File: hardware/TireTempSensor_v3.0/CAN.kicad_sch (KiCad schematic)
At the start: 14 parts, among them U7 ADM3057ExRW

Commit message: Poprawki, kontynuacja layoutu
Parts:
- C32, C38: value 100n -> 47u
- C35: value 220n -> 47u
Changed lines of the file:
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@@
 	(polyline
 		(pts
-			(xy 108.585 17.145) (xy 107.95 193.04)
+			(xy 108.585 45.085) (xy 108.585 104.14)
 		)
 		(stroke
@@
 			)
 		)
-		(property "Value" "100n"
+		(property "Value" "47u"
 			(at 150.5013 22.225 90)
 			(effects
@@
 			)
 		)
-		(property "Value" "220n"
+		(property "Value" "47u"
 			(at 85.725 79.3685 0)
 			(effects
@@
 			)
 		)
-		(property "Value" "100n"
+		(property "Value" "47u"
 			(at 118.7513 22.225 90)
 			(effects

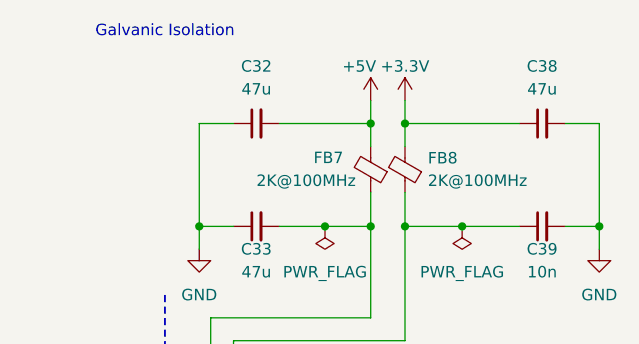
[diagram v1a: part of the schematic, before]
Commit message: Nowy layout, nowe tvsy
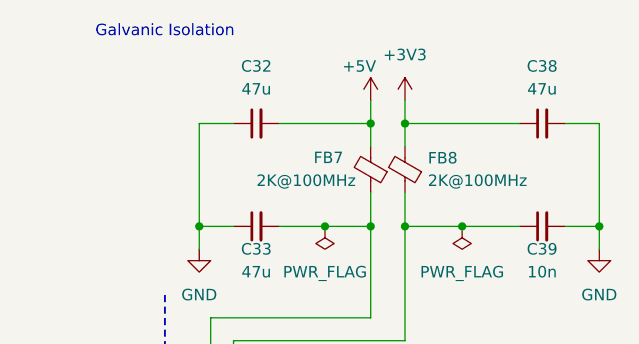
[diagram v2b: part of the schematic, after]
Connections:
- net +3.3V renamed +3V3
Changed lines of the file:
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@@
+	)
+	(symbol
+		(lib_id "power:+3V3")
+		(at 135.255 23.495 0)
+		(unit 1)
+		(exclude_from_sim no)
+		(in_bom yes)
+		(on_board yes)
+		(dnp no)
+		(fields_autoplaced yes)
+		(property "Reference" "#PWR0119"
+			(at 135.255 27.305 0)
+			(effects
+				(font
+					(size 1.27 1.27)
+				)
+				(hide yes)
+			)
+		)
+		(property "Value" "+3V3"
+			(at 135.255 18.415 0)
+			(effects
+				(font
+					(size 1.27 1.27)
+				)
+			)
+		)
+		(property "Footprint" ""
+			(at 135.255 23.495 0)
+			(effects
+				(font
+					(size 1.27 1.27)
+				)
+				(hide yes)
+			)
+		)
+		(property "Datasheet" ""
+			(at 135.255 23.495 0)
+			(effects
+				(font
+					(size 1.27 1.27)
+				)
+				(hide yes)
+			)
+		)
+		(property "Description" ""
+			(at 135.255 23.495 0)
+			(effects
+				(font
+					(size 1.27 1.27)
+				)
+			)
+		)
+		(pin "1"
+		)
+		(instances
+			(project "TireTempSensor_v2.0"
+				(path "/6e95e1be-fdd6-40ae-a4f8-5c53e6058d6c/4ba3e466-bd12-480c-9adb-36d880e66258"
+					(reference "#PWR0119")
+					(unit 1)
+				)
+			)
+		)
 	)
 	(symbol
@@
 					(unit 1)
 				)
-			)
-		)
-	)
-	(symbol
-		(lib_id "power:+3.3V")
-		(at 135.255 23.495 0)
-		(unit 1)
-		(exclude_from_sim no)
-		(in_bom yes)
-		(on_board yes)
-		(dnp no)
-		(fields_autoplaced yes)
-		(property "Reference" "#PWR062"
-			(at 135.255 27.305 0)
-			(effects
-				(font
-					(size 1.27 1.27)
-				)
-				(hide yes)
-			)
-		)
-		(property "Value" "+3.3V"
-			(at 135.255 19.685 0)
-			(effects
-				(font
-					(size 1.27 1.27)
-				)
-			)
-		)
-		(property "Footprint" ""
-			(at 135.255 23.495 0)
-			(effects
-				(font
-					(size 1.27 1.27)
-				)
-				(hide yes)
-			)
-		)
-		(property "Datasheet" ""
-			(at 135.255 23.495 0)
-			(effects
-				(font
-					(size 1.27 1.27)
-				)
-				(hide yes)
-			)
-		)
-		(property "Description" ""
-			(at 135.255 23.495 0)
-			(effects
-				(font
-					(size 1.27 1.27)
-				)
-				(hide yes)
-			)
-		)
-		(pin "1"
-		)
-		(instances
-			(project "TireTempSensor_v2.0"
-				(path "/6e95e1be-fdd6-40ae-a4f8-5c53e6058d6c/4ba3e466-bd12-480c-9adb-36d880e66258"
-					(reference "#PWR062")
-					(unit 1)
-				)

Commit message: Poprawione :3
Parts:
- C32, C33, C34, C38: footprint Capacitor_SMD:C_0603_1608Metric_Pad1.08x0.95mm_HandSolder -> Capacitor_SMD:C_0805_2012Metric_Pad1.18x1.45mm_HandSolder
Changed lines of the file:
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@@
 			)
 		)
-		(property "Footprint" "Capacitor_SMD:C_0603_1608Metric_Pad1.08x0.95mm_HandSolder"
+		(property "Footprint" "Capacitor_SMD:C_0805_2012Metric_Pad1.18x1.45mm_HandSolder"
 			(at 118.745 37.465 0)
 			(effects
@@
 			)
 		)
-		(property "Footprint" "Capacitor_SMD:C_0603_1608Metric_Pad1.08x0.95mm_HandSolder"
+		(property "Footprint" "Capacitor_SMD:C_0805_2012Metric_Pad1.18x1.45mm_HandSolder"
 			(at 150.495 26.035 0)
 			(effects
@@
 			)
 		)
-		(property "Footprint" "Capacitor_SMD:C_0603_1608Metric_Pad1.08x0.95mm_HandSolder"
+		(property "Footprint" "Capacitor_SMD:C_0805_2012Metric_Pad1.18x1.45mm_HandSolder"
 			(at 65.405 78.105 0)
 			(effects
@@
 			)
 		)
-		(property "Footprint" "Capacitor_SMD:C_0603_1608Metric_Pad1.08x0.95mm_HandSolder"
+		(property "Footprint" "Capacitor_SMD:C_0805_2012Metric_Pad1.18x1.45mm_HandSolder"
 			(at 118.745 26.035 0)
 			(effects

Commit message: Piotrkowe poprawy
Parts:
- FB5, FB6, FB7, FB8: footprint Inductor_SMD:L_0603_1608Metric_Pad1.05x0.95mm_HandSolder -> Inductor_SMD:L_0805_2012Metric_Pad1.05x1.20mm_HandSolder
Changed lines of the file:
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@@
 			)
 		)
-		(property "Footprint" "Inductor_SMD:L_0603_1608Metric_Pad1.05x0.95mm_HandSolder"
+		(property "Footprint" "Inductor_SMD:L_0805_2012Metric_Pad1.05x1.20mm_HandSolder"
 			(at 137.033 31.115 90)
 			(effects
@@
 			)
 		)
-		(property "Datasheet" "https://www.mouser.pl/ProductDetail/Eaton-Electronics/MFBW1V1608-202-R?qs=W%2FMpXkg%252BdQ4ShGRk3jgFwA%3D%3D"
+		(property "Datasheet" "https://www.mouser.pl/ProductDetail/Fair-Rite/2508052027Y1?qs=paL1wOLBYNcCgyNDp2sTMQ%3D%3D"
 			(at 135.255 31.115 0)
 			(effects
@@
 			)
 		)
-		(property "Footprint" "Inductor_SMD:L_0603_1608Metric_Pad1.05x0.95mm_HandSolder"
+		(property "Footprint" "Inductor_SMD:L_0805_2012Metric_Pad1.05x1.20mm_HandSolder"
 			(at 133.223 31.115 90)
 			(effects
@@
 			)
 		)
-		(property "Datasheet" "https://www.mouser.pl/ProductDetail/Eaton-Electronics/MFBW1V1608-202-R?qs=W%2FMpXkg%252BdQ4ShGRk3jgFwA%3D%3D"
+		(property "Datasheet" "https://www.mouser.pl/ProductDetail/Fair-Rite/2508052027Y1?qs=paL1wOLBYNcCgyNDp2sTMQ%3D%3D"
 			(at 131.445 31.115 0)
 			(effects
@@
 					(size 1.27 1.27)
 				)
-			)
-		)
-		(property "Footprint" "Inductor_SMD:L_0603_1608Metric_Pad1.05x0.95mm_HandSolder"
+				(justify right)
+			)
+		)
+		(property "Footprint" "Inductor_SMD:L_0805_2012Metric_Pad1.05x1.20mm_HandSolder"
 			(at 74.295 77.343 90)
 			(effects
@@
 			)
 		)
-		(property "Datasheet" "https://www.mouser.pl/ProductDetail/Eaton-Electronics/MFBW1V1608-202-R?qs=W%2FMpXkg%252BdQ4ShGRk3jgFwA%3D%3D"
+		(property "Datasheet" "https://www.mouser.pl/ProductDetail/Fair-Rite/2508052027Y1?qs=paL1wOLBYNcCgyNDp2sTMQ%3D%3D"
 			(at 74.295 75.565 0)
 			(effects
@@
 		)
 		(property "Value" "2K@100MHz"
-			(at 73.025 84.455 90)
-			(effects
-				(font
-					(size 1.27 1.27)
-				)
-			)
-		)
-		(property "Footprint" "Inductor_SMD:L_0603_1608Metric_Pad1.05x0.95mm_HandSolder"
+			(at 67.945 84.455 90)
+			(effects
+				(font
+					(size 1.27 1.27)
+				)
+				(justify right)
+			)
+		)
+		(property "Footprint" "Inductor_SMD:L_0805_2012Metric_Pad1.05x1.20mm_HandSolder"
 			(at 74.295 82.423 90)
 			(effects
@@
 			)
 		)
-		(property "Datasheet" "https://www.mouser.pl/ProductDetail/Eaton-Electronics/MFBW1V1608-202-R?qs=W%2FMpXkg%252BdQ4ShGRk3jgFwA%3D%3D"
+		(property "Datasheet" "https://www.mouser.pl/ProductDetail/Fair-Rite/2508052027Y1?qs=paL1wOLBYNcCgyNDp2sTMQ%3D%3D"
 			(at 74.295 80.645 0)
 			(effects

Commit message: Z wielkim bólem przesunięte złącze aby poprawić routing cana
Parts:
- C35: footprint Capacitor_SMD:C_0603_1608Metric_Pad1.08x0.95mm_HandSolder -> Capacitor_SMD:C_0805_2012Metric_Pad1.18x1.45mm_HandSolder
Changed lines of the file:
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@@
 			)
 		)
-		(property "Footprint" "Capacitor_SMD:C_0603_1608Metric_Pad1.08x0.95mm_HandSolder"
+		(property "Footprint" "Capacitor_SMD:C_0805_2012Metric_Pad1.18x1.45mm_HandSolder"
 			(at 83.185 78.105 0)
 			(effects

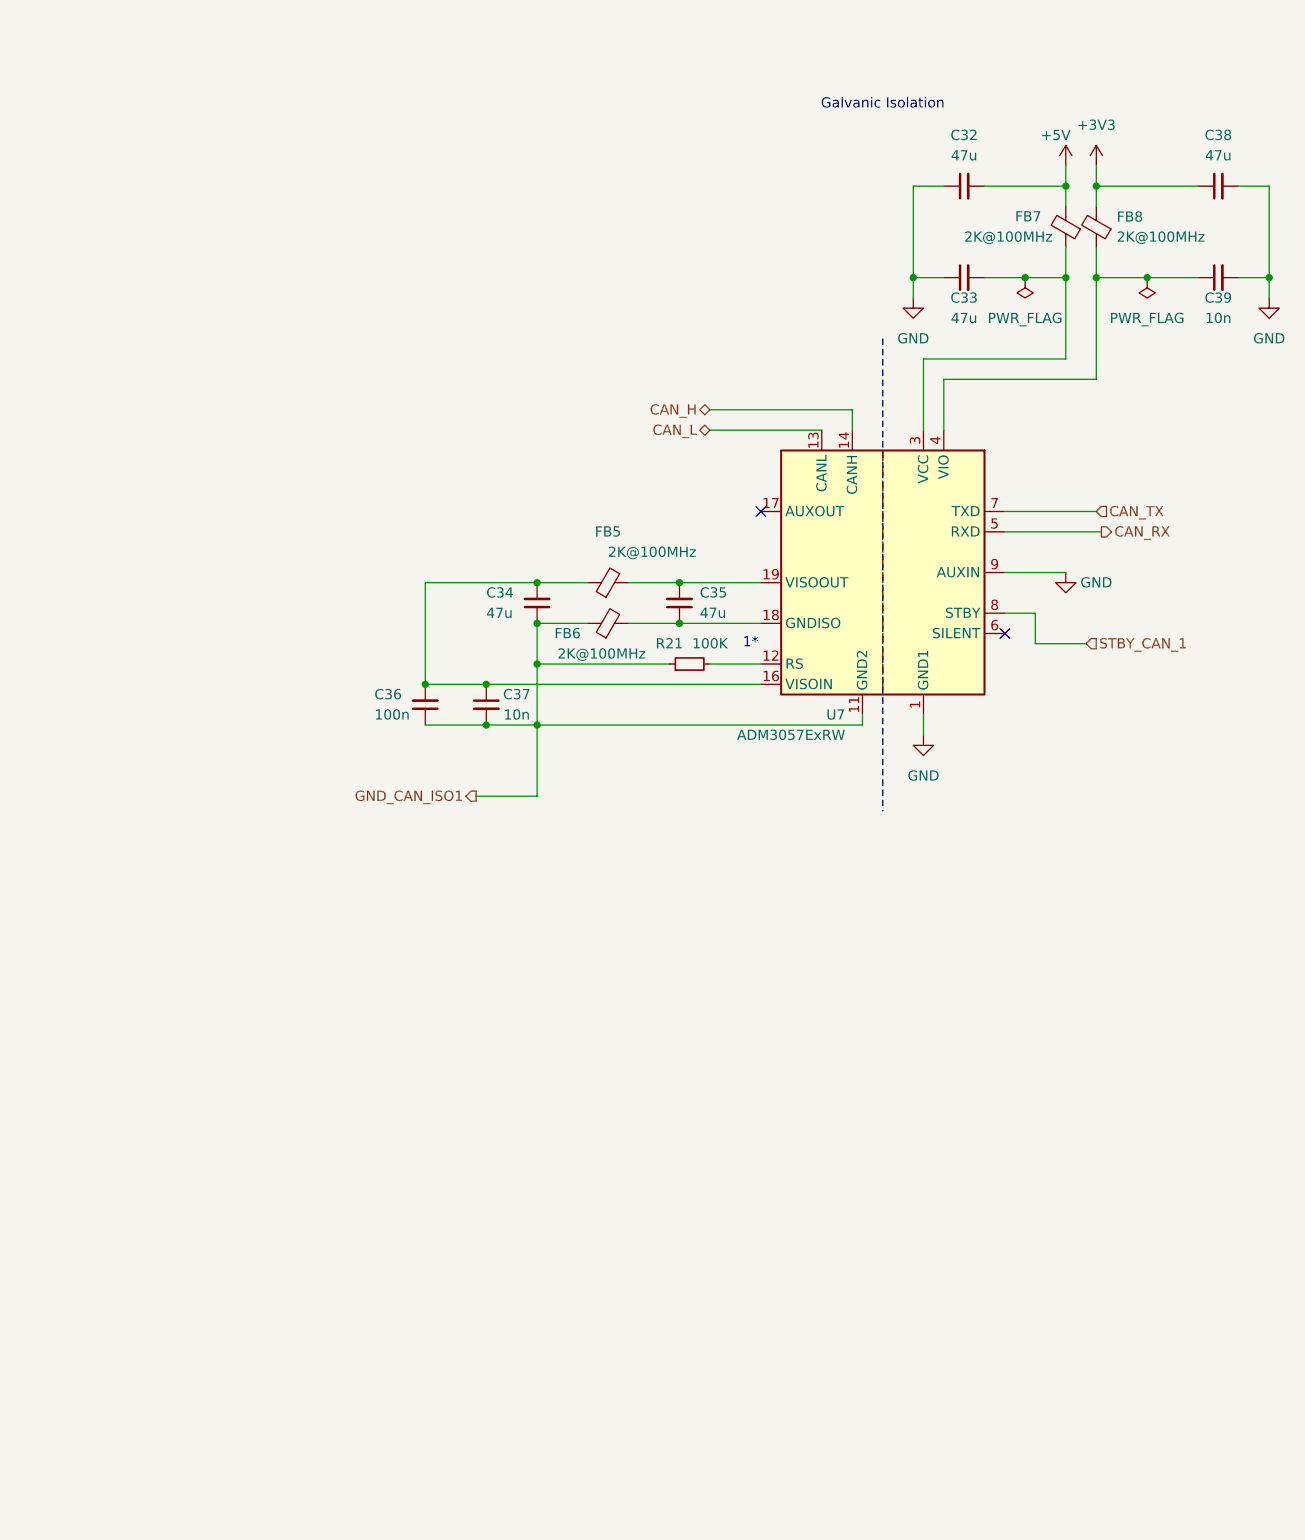
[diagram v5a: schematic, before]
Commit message: Added aditional emi prevention measures
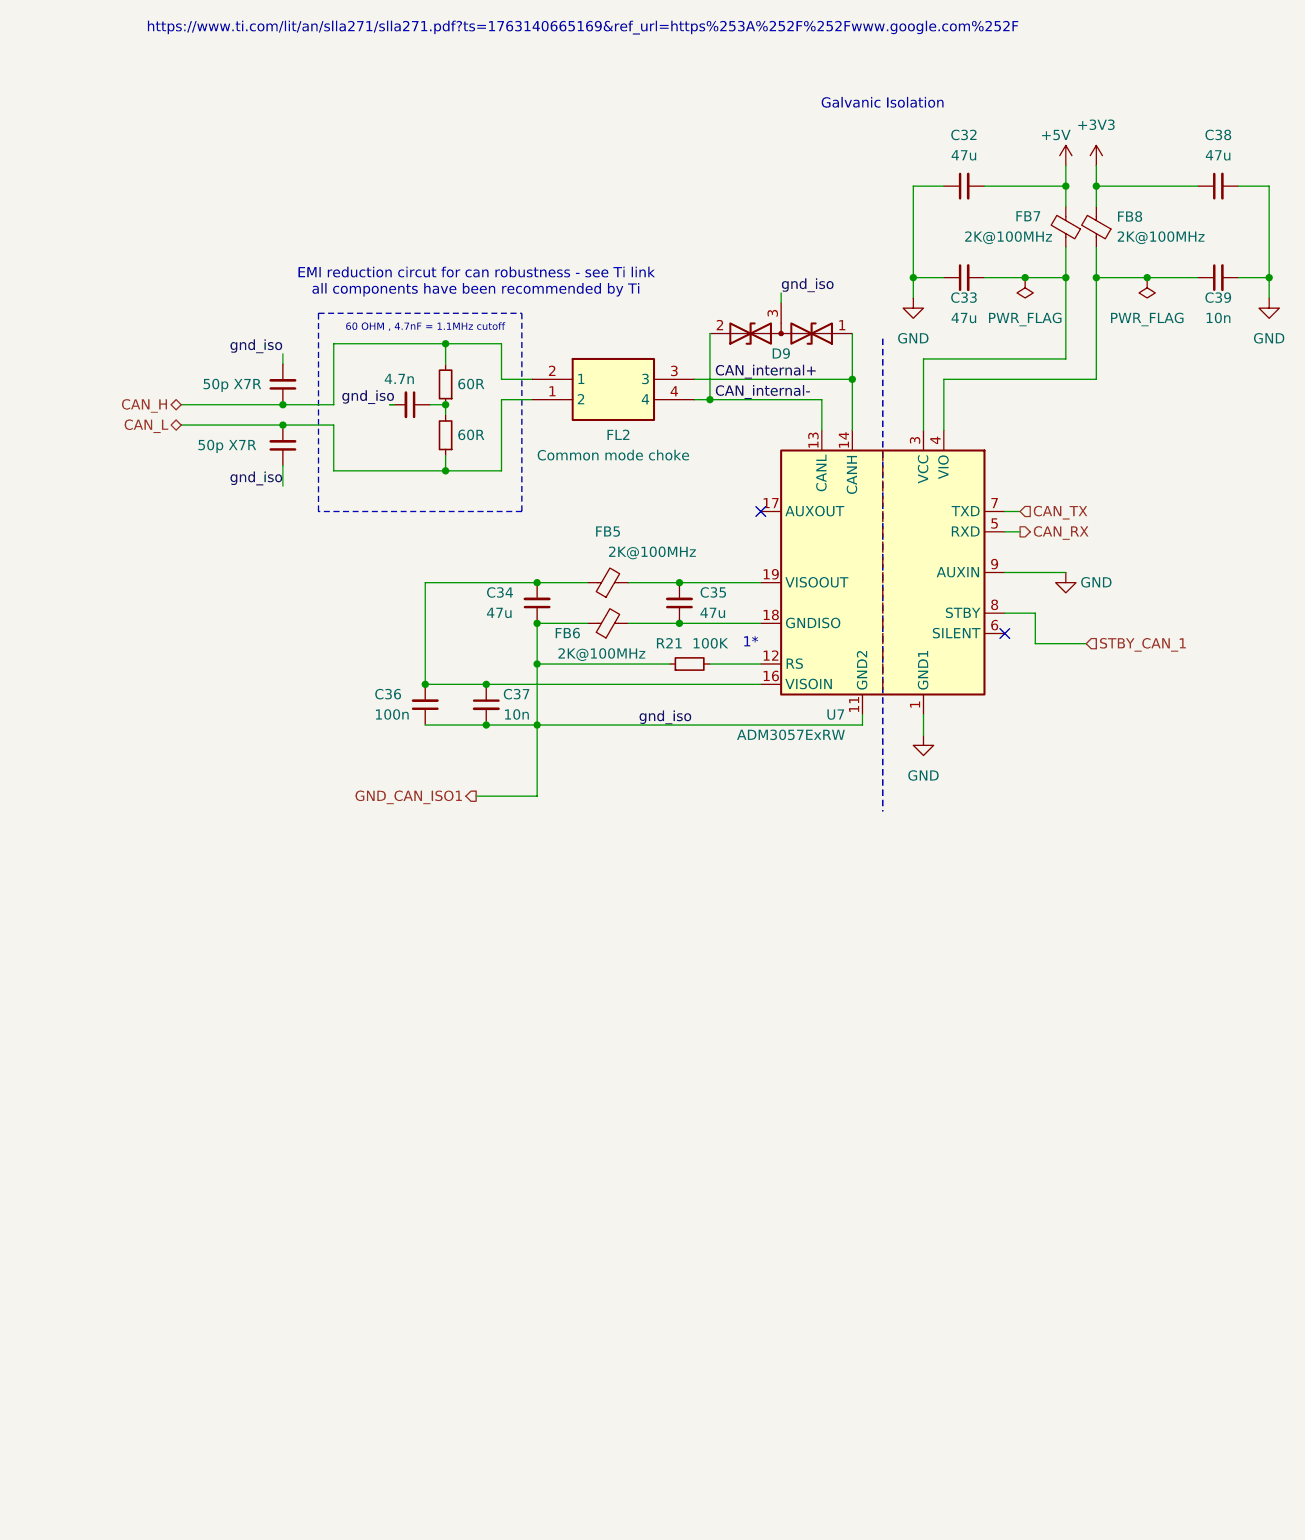
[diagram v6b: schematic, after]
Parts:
- added C44: 4.7n, Capacitor_SMD:C_0805_2012Metric_Pad1.18x1.45mm_HandSolder, symbol Device:C_Small
- added C50, C51: 50p X7R, Capacitor_SMD:C_0805_2012Metric_Pad1.18x1.45mm_HandSolder, symbol Device:C_Small
- added D9: D_TVS_Dual_AAC, Package_TO_SOT_SMD:SOT-23_Handsoldering, symbol Device:D_TVS_Dual_AAC
- added FL2: Common mode choke, footprint:DR331513BE, symbol DR331-513AE:DR331-513AE
- added R25, R26: 60R, Resistor_SMD:R_0603_1608Metric_Pad0.98x0.95mm_HandSolder, symbol Device:R_Small
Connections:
- net CAN_H: now also C51.1, FL2.2 (1), R25.2; no longer U7.14 (CANH)
- net CAN_L: now also C50.2, FL2.1 (2), R26.1; no longer U7.13 (CANL)
- net GND_CAN_ISO1: now also C44.2, C50.1, C51.2, D9.3 (common)
- new net: C44.1, R25.1, R26.2
- new net CAN_internal+: D9.1 (A1), FL2.3, U7.14 (CANH)
- new net CAN_internal-: D9.2 (A2), FL2.4, U7.13 (CANL)
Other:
- note added: "60 OHM , 4.7nF = 1.1MHz cutoff"
- note added: "EMI reduction circut for can robustness - see Ti link all components have been recommended by Ti"
- note added: "https://www.ti.com/lit/an/slla271/slla271.pdf?ts=1763140665169&ref_url=https%253A%252F%252Fwww.google.com%252F"
